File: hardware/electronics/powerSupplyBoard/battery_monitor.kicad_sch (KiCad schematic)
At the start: 31 parts, among them Q2 CSD18532Q5B, Q3 CSD18532Q5B, U2 BQ76905

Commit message: renamed bms board to power supply board
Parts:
- D2, D3, D4: footprint (none) -> DS-Package-SO:SOD123
- Q2, Q3: footprint (none) -> DS-Package-SO:SON8P127_500X600X100L56X41N
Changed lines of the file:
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@@
 		)
 		(instances
-			(project "bms_breakout"
+			(project "powerSupplyBoard"
 				(path "/6f3ae1d2-e925-4178-b812-ea14ec542b6c/ec26ef98-8e8c-46d6-a822-e7ed17aae681"
 					(reference "R17")
@@
 		)
 		(instances
-			(project "bms_breakout"
+			(project "powerSupplyBoard"
 				(path "/6f3ae1d2-e925-4178-b812-ea14ec542b6c/ec26ef98-8e8c-46d6-a822-e7ed17aae681"
 					(reference "C27")
@@
 		)
 		(instances
-			(project "bms_breakout"
+			(project "powerSupplyBoard"
 				(path "/6f3ae1d2-e925-4178-b812-ea14ec542b6c/ec26ef98-8e8c-46d6-a822-e7ed17aae681"
 					(reference "R12")
@@
 		)
 		(instances
-			(project "bms_breakout"
+			(project "powerSupplyBoard"
 				(path "/6f3ae1d2-e925-4178-b812-ea14ec542b6c/ec26ef98-8e8c-46d6-a822-e7ed17aae681"
 					(reference "#PWR018")
@@
 		)
 		(instances
-			(project "bms_breakout"
+			(project "powerSupplyBoard"
 				(path "/6f3ae1d2-e925-4178-b812-ea14ec542b6c/ec26ef98-8e8c-46d6-a822-e7ed17aae681"
 					(reference "C23")
@@
 		)
 		(instances
-			(project "bms_breakout"
+			(project "powerSupplyBoard"
 				(path "/6f3ae1d2-e925-4178-b812-ea14ec542b6c/ec26ef98-8e8c-46d6-a822-e7ed17aae681"
 					(reference "#PWR019")
@@
 		)
 		(instances
-			(project "bms_breakout"
+			(project "powerSupplyBoard"
 				(path "/6f3ae1d2-e925-4178-b812-ea14ec542b6c/ec26ef98-8e8c-46d6-a822-e7ed17aae681"
 					(reference "R14")
@@
 		)
 		(instances
-			(project "bms_breakout"
+			(project "powerSupplyBoard"
 				(path "/6f3ae1d2-e925-4178-b812-ea14ec542b6c/ec26ef98-8e8c-46d6-a822-e7ed17aae681"
 					(reference "#PWR020")
@@
 		)
 		(instances
-			(project "bms_breakout"
+			(project "powerSupplyBoard"
 				(path "/6f3ae1d2-e925-4178-b812-ea14ec542b6c/ec26ef98-8e8c-46d6-a822-e7ed17aae681"
 					(reference "C24")
@@
 		)
 		(instances
-			(project "bms_breakout"
+			(project "powerSupplyBoard"
 				(path "/6f3ae1d2-e925-4178-b812-ea14ec542b6c/ec26ef98-8e8c-46d6-a822-e7ed17aae681"
 					(reference "R11")
@@
 		)
 		(instances
-			(project "bms_breakout"
+			(project "powerSupplyBoard"
 				(path "/6f3ae1d2-e925-4178-b812-ea14ec542b6c/ec26ef98-8e8c-46d6-a822-e7ed17aae681"
 					(reference "C26")
@@
 		)
 		(instances
-			(project "bms_breakout"
+			(project "powerSupplyBoard"
 				(path "/6f3ae1d2-e925-4178-b812-ea14ec542b6c/ec26ef98-8e8c-46d6-a822-e7ed17aae681"
 					(reference "R9")
@@
 		)
 		(instances
-			(project "bms_breakout"
+			(project "powerSupplyBoard"
 				(path "/6f3ae1d2-e925-4178-b812-ea14ec542b6c/ec26ef98-8e8c-46d6-a822-e7ed17aae681"
 					(reference "C28")
@@
 			)
 		)
-		(property "Footprint" ""
+		(property "Footprint" "DS-Package-SO:SOD123"
 			(at 207.01 121.92 90)
 			(effects
@@
 		)
 		(instances
-			(project "bms_breakout"
+			(project "powerSupplyBoard"
 				(path "/6f3ae1d2-e925-4178-b812-ea14ec542b6c/ec26ef98-8e8c-46d6-a822-e7ed17aae681"
 					(reference "D4")
@@
 		)
 		(instances
-			(project "bms_breakout"
+			(project "powerSupplyBoard"
 				(path "/6f3ae1d2-e925-4178-b812-ea14ec542b6c/ec26ef98-8e8c-46d6-a822-e7ed17aae681"
 					(reference "R21")
@@
 		)
 		(instances
-			(project "bms_breakout"
+			(project "powerSupplyBoard"
 				(path "/6f3ae1d2-e925-4178-b812-ea14ec542b6c/ec26ef98-8e8c-46d6-a822-e7ed17aae681"
 					(reference "R13")
@@
 		)
 		(instances
-			(project "bms_breakout"
+			(project "powerSupplyBoard"
 				(path "/6f3ae1d2-e925-4178-b812-ea14ec542b6c/ec26ef98-8e8c-46d6-a822-e7ed17aae681"
 					(reference "R20")
@@
 			)
 		)
-		(property "Footprint" ""
+		(property "Footprint" "DS-Package-SO:SOD123"
 			(at 161.29 88.9 0)
 			(effects
@@
 		)
 		(instances
-			(project "bms_breakout"
+			(project "powerSupplyBoard"
 				(path "/6f3ae1d2-e925-4178-b812-ea14ec542b6c/ec26ef98-8e8c-46d6-a822-e7ed17aae681"
 					(reference "D3")
@@
 		)
 		(instances
-			(project "bms_breakout"
+			(project "powerSupplyBoard"
 				(path "/6f3ae1d2-e925-4178-b812-ea14ec542b6c/ec26ef98-8e8c-46d6-a822-e7ed17aae681"
 					(reference "C21")
@@
 		)
 		(instances
-			(project "bms_breakout"
+			(project "powerSupplyBoard"
 				(path "/6f3ae1d2-e925-4178-b812-ea14ec542b6c/ec26ef98-8e8c-46d6-a822-e7ed17aae681"
 					(reference "R15")
@@
 		)
 		(instances
-			(project "bms_breakout"
+			(project "powerSupplyBoard"
 				(path "/6f3ae1d2-e925-4178-b812-ea14ec542b6c/ec26ef98-8e8c-46d6-a822-e7ed17aae681"
 					(reference "#PWR022")
@@
 		)
 		(instances
-			(project "bms_breakout"
+			(project "powerSupplyBoard"
 				(path "/6f3ae1d2-e925-4178-b812-ea14ec542b6c/ec26ef98-8e8c-46d6-a822-e7ed17aae681"
 					(reference "#PWR021")
@@
 		)
 		(instances
-			(project "bms_breakout"
+			(project "powerSupplyBoard"
 				(path "/6f3ae1d2-e925-4178-b812-ea14ec542b6c/ec26ef98-8e8c-46d6-a822-e7ed17aae681"
 					(reference "R10")
@@
 			)
 		)
-		(property "Footprint" ""
+		(property "Footprint" "DS-Package-SO:SOD123"
 			(at 161.29 81.28 0)
 			(effects
@@
 		)
 		(instances
-			(project "bms_breakout"
+			(project "powerSupplyBoard"
 				(path "/6f3ae1d2-e925-4178-b812-ea14ec542b6c/ec26ef98-8e8c-46d6-a822-e7ed17aae681"
 					(reference "R18")
@@
 		)
 		(instances
-			(project "bms_breakout"
+			(project "powerSupplyBoard"
 				(path "/6f3ae1d2-e925-4178-b812-ea14ec542b6c/ec26ef98-8e8c-46d6-a822-e7ed17aae681"
 					(reference "C25")
@@
 		)
 		(instances
-			(project "bms_breakout"
+			(project "powerSupplyBoard"
 				(path "/6f3ae1d2-e925-4178-b812-ea14ec542b6c/ec26ef98-8e8c-46d6-a822-e7ed17aae681"
 					(reference "C30")
@@
 	)
 	(symbol
+		(lib_name "DS-Transistors:NMOS_SGD_PWR")
 		(lib_id "DS-Transistors:NMOS_SGD_PWR")
 		(at 190.5 125.73 0)
@@
 			)
 		)
-		(property "Footprint" ""
+		(property "Footprint" "DS-Package-SO:SON8P127_500X600X100L56X41N"
 			(at 192.405 128.27 90)
 			(effects
@@
 		)
 		(instances
-			(project "bms_breakout"
+			(project "powerSupplyBoard"
 				(path "/6f3ae1d2-e925-4178-b812-ea14ec542b6c/ec26ef98-8e8c-46d6-a822-e7ed17aae681"
 					(reference "R16")
@@
 		)
 		(instances
-			(project "bms_breakout"
+			(project "powerSupplyBoard"
 				(path "/6f3ae1d2-e925-4178-b812-ea14ec542b6c/ec26ef98-8e8c-46d6-a822-e7ed17aae681"
 					(reference "R19")
@@
 		)
 		(instances
-			(project "bms_breakout"
+			(project "powerSupplyBoard"
 				(path "/6f3ae1d2-e925-4178-b812-ea14ec542b6c/ec26ef98-8e8c-46d6-a822-e7ed17aae681"
 					(reference "C29")
@@
 	)
 	(symbol
+		(lib_name "DS-Transistors:NMOS_SGD_PWR")
 		(lib_id "DS-Transistors:NMOS_SGD_PWR")
 		(at 177.8 125.73 180)
@@
 			)
 		)
-		(property "Footprint" ""
+		(property "Footprint" "DS-Package-SO:SON8P127_500X600X100L56X41N"
 			(at 175.895 128.27 90)
 			(effects
@@
 		)
 		(instances
-			(project "bms_breakout"
+			(project "powerSupplyBoard"
 				(path "/6f3ae1d2-e925-4178-b812-ea14ec542b6c/ec26ef98-8e8c-46d6-a822-e7ed17aae681"
 					(reference "Q2")

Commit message: added footprint for BQ76905
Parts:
- U2: footprint (none) -> DS-PMIC-SMD:RGR0020A
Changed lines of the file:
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@@
 			)
 		)
-		(property "Footprint" ""
+		(property "Footprint" "DS-PMIC-SMD:RGR0020A"
 			(at 127 101.6 0)
 			(effects
@@
 	)
 	(symbol
-		(lib_name "DS-Transistors:NMOS_SGD_PWR")
 		(lib_id "DS-Transistors:NMOS_SGD_PWR")
 		(at 190.5 125.73 0)
@@
 	)
 	(symbol
-		(lib_name "DS-Transistors:NMOS_SGD_PWR")
 		(lib_id "DS-Transistors:NMOS_SGD_PWR")
 		(at 177.8 125.73 180)

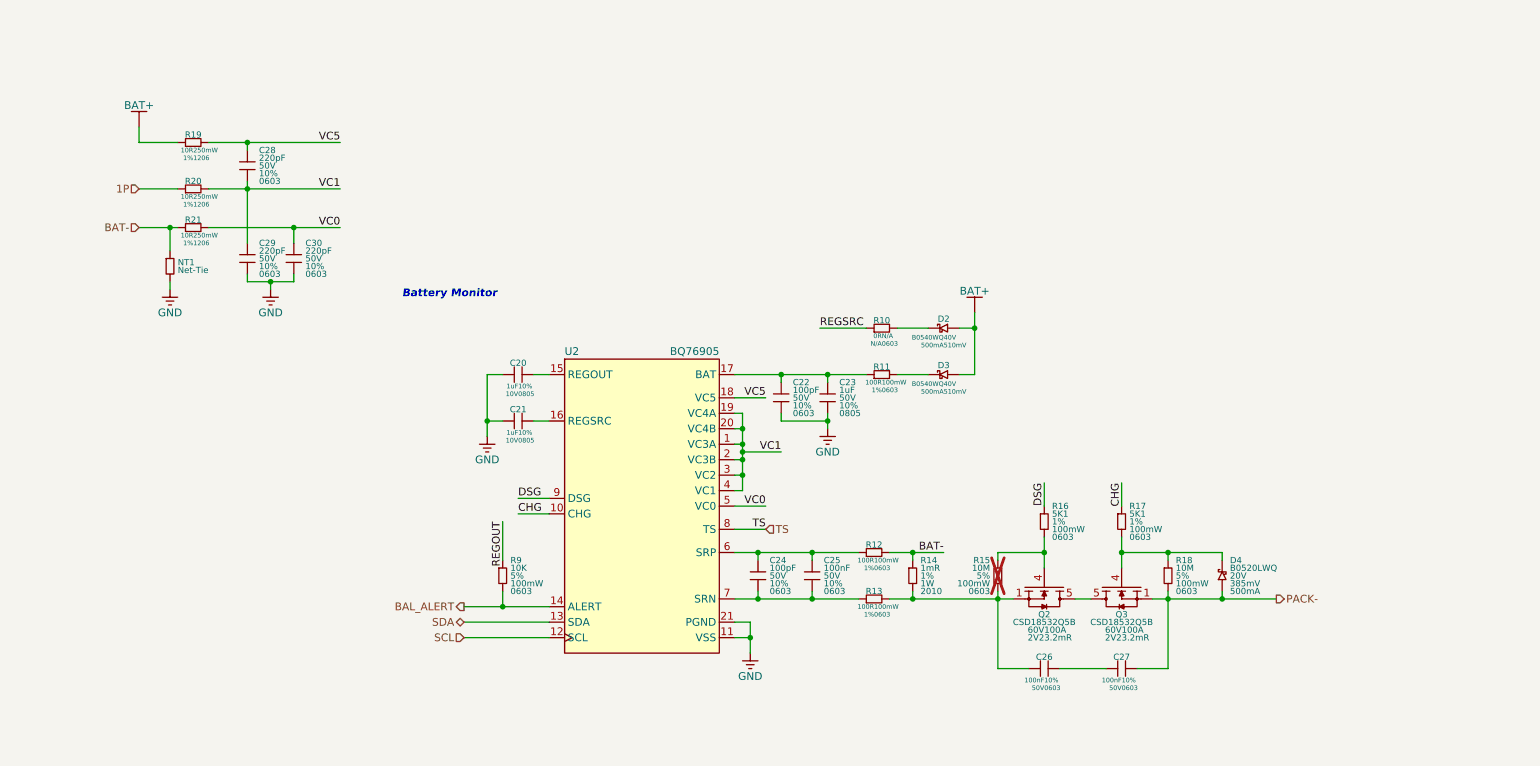
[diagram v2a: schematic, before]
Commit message: renumbers passives and cleaned up sheets
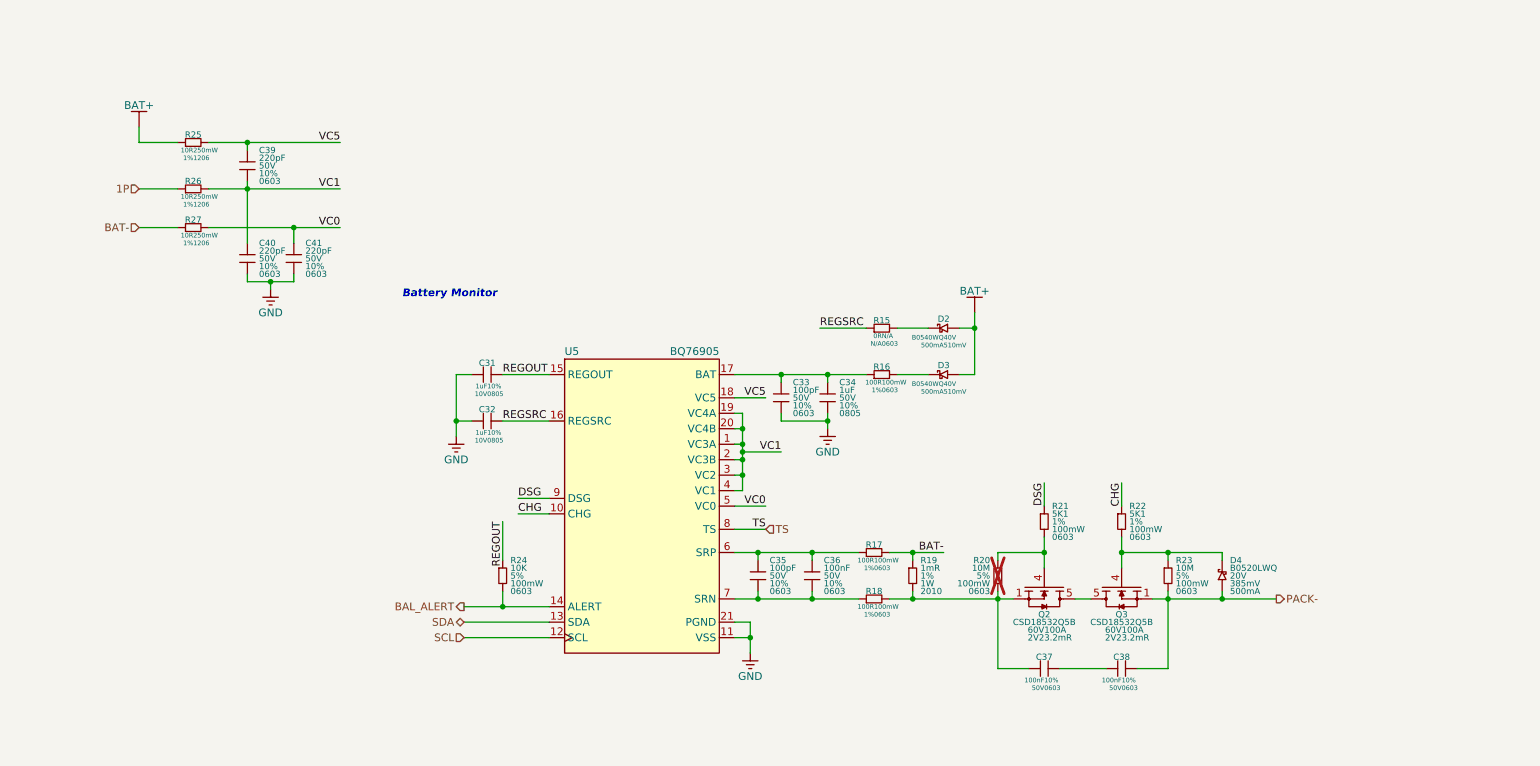
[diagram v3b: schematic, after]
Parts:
- removed D4: B0520LWQ, DS-Package-SO:SOD123, symbol DSE-Passives:D_Schottky
- removed NT1: Net-Tie, symbol DS-Passives:NT
- added D4: B0520LWQ, DS-Package-SO:SOD123, symbol lib_sch:D_Schottky
- C31: renamed from C20; symbol DS-Passives:C_horizontal -> lib_sch:C_horizontal
- C32: renamed from C21; symbol DS-Passives:C_horizontal -> lib_sch:C_horizontal
- C33: renamed from C22; symbol DS-Passives:C -> lib_sch:C
- C34: renamed from C23; symbol DS-Passives:C -> lib_sch:C
- C35: renamed from C24; symbol DS-Passives:C -> lib_sch:C
- C36: renamed from C25; symbol DS-Passives:C -> lib_sch:C_2
- C37: renamed from C26; symbol DS-Passives:C_horizontal -> lib_sch:C_horizontal
- C38: renamed from C27; symbol DS-Passives:C_horizontal -> lib_sch:C_horizontal
- C39: renamed from C28; symbol DS-Passives:C -> lib_sch:C
- C40: renamed from C29; symbol DS-Passives:C -> lib_sch:C
- C41: renamed from C30; symbol DS-Passives:C -> lib_sch:C
- D2, D3: symbol DS-Passives:D_Schottky_horizontal -> lib_sch:D_Schottky_horizontal
- Q2: symbol DS-Transistors:NMOS_SGD_PWR -> lib_sch:NMOS_SGD_PWR_1
- Q3: symbol DS-Transistors:NMOS_SGD_PWR -> lib_sch:NMOS_SGD_PWR
- R15: renamed from R10; symbol DS-Passives:R_horizontal -> lib_sch:R_horizontal
- R16: renamed from R11; symbol DS-Passives:R_horizontal -> lib_sch:R_horizontal
- R17: renamed from R12; symbol DS-Passives:R_horizontal -> lib_sch:R_horizontal
- R18: renamed from R13; symbol DS-Passives:R_horizontal -> lib_sch:R_horizontal
- R19: renamed from R14; symbol DS-Passives:R -> lib_sch:R
- R20: renamed from R15; symbol DS-Passives:R -> lib_sch:R
- R21: renamed from R16; symbol DS-Passives:R -> lib_sch:R
- R22: renamed from R17; symbol DS-Passives:R -> lib_sch:R
- R23: renamed from R18; symbol DS-Passives:R -> lib_sch:R
- R24: renamed from R9; symbol DS-Passives:R -> lib_sch:R
- R25: renamed from R19; footprint (none) -> DS-Resistors-SMD:CRCW1206; symbol DS-Passives:R_horizontal -> lib_sch:R_horizontal
- R26: renamed from R20; footprint (none) -> DS-Resistors-SMD:CRCW1206; symbol DS-Passives:R_horizontal -> lib_sch:R_horizontal
- R27: renamed from R21; footprint (none) -> DS-Resistors-SMD:CRCW1206; symbol DS-Passives:R_horizontal -> lib_sch:R_horizontal
- U5: renamed from U2; symbol DS-PMIC:BQ76905 -> lib_sch:BQ76905
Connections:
- net PACK-: now also D4.1
- net REGOUT: now also C31.2, U5.15 (REGOUT)
- net REGSRC: now also C32.2, U5.16 (REGSRC)
- net at Q3.4, R22.2, R23.1: now also D4.2
- net at Q2.5, Q2.6, Q2.7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: now also Q2.8, Q3.8
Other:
- moved on the sheet: C31, C32

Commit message: fixed schematic, organized page, and fixed ground nets
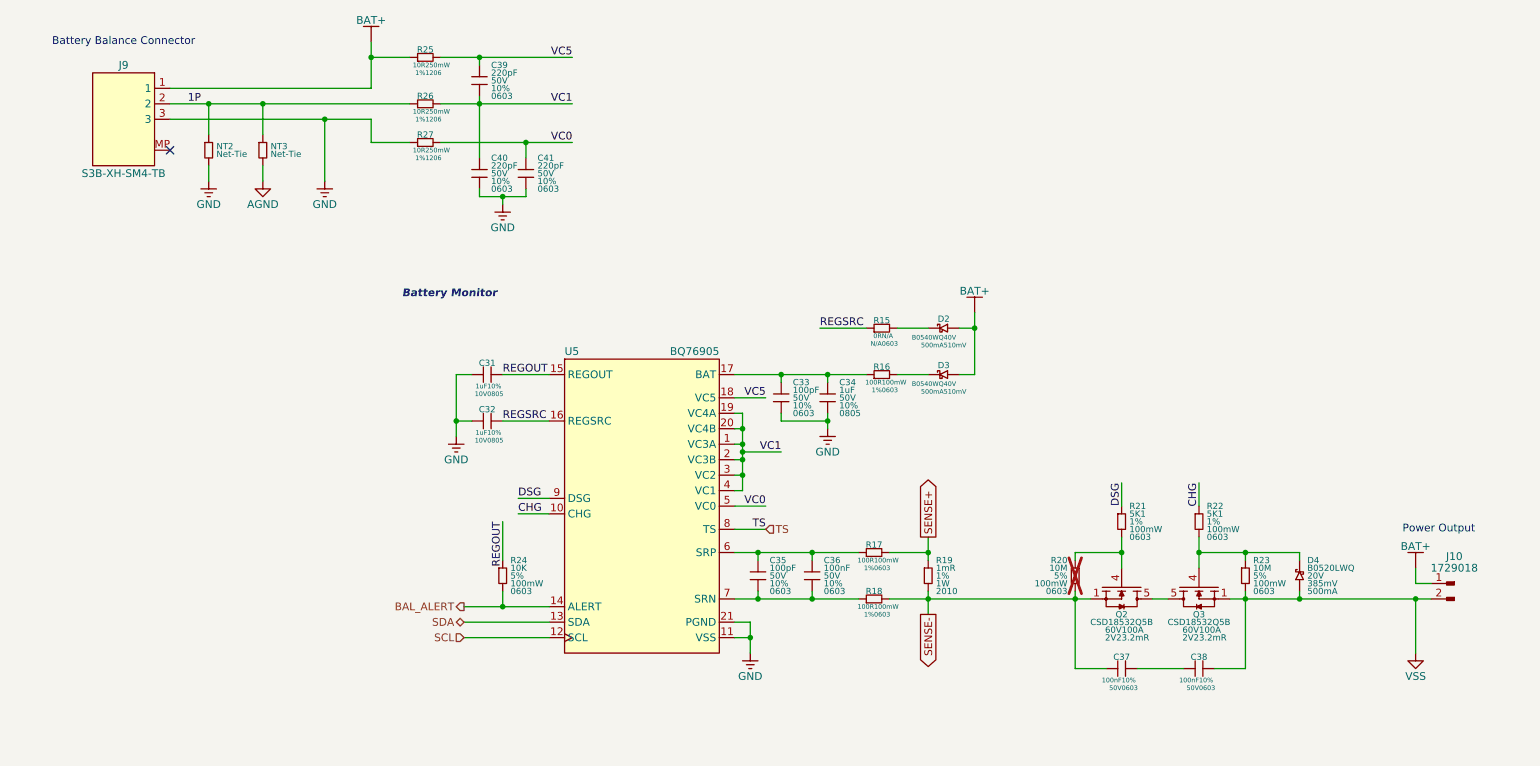
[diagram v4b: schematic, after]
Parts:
- added J10: 1729018, DS-Rectangular-Connectors:5mmTerminalBlock, symbol lib_sch:Conn_01x02_Pin
- added J9: S3B-XH-SM4-TB, DS-Rectangular-Connectors:JST_XH_S3B-SM4-TB, symbol lib_sch:S3B-PH-SM4-TB
- added NT2, NT3: Net-Tie, DS-Resistors-SMD:CRCW1210, symbol lib_sch:NT
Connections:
- net 1P: now also J9.2, NT2.1, NT3.1
- net BAT+: now also J10.1, J9.1
- net GND: now also R27.1, J9.3, NT2.2
- net SENSE-: now reaches C37.1, Q2.1, Q2.2, Q2.3, R18.2, R19.2, R20.2
- net BAT- renamed SENSE+
- net SENSE+: no longer R27.1
- net PACK- renamed VSS
- net VSS: now also J10.2
- new net AGND: NT3.2
- no-connect marks 0 -> 1
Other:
- note added: "Battery Balance Connector"
- note added: "Power Output"
- moved on the sheet: C37, C38, C39, C40, C41, D4, Q2, Q3, R19, R20, R21, R22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
